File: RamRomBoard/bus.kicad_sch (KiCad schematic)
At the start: 4 parts, among them J1 BUS, J2 BUS, J3 Spare, J4 Spare

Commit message: New XC9572 Example
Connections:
- net RES6 is gone; now on net ~{CE_EXT1}: J2.5 (Pin_5), J4.5 (Pin_5)
- net RES0: now also J2.23 (Pin_23), J4.23 (Pin_23); no longer J2.11 (Pin_11), J4.11 (Pin_11)
- net RES1: now also J2.24 (Pin_24), J4.24 (Pin_24); no longer J2.10 (Pin_10), J4.10 (Pin_10)
- net RES2: now also J2.21 (Pin_21), J4.21 (Pin_21); no longer J2.9 (Pin_9), J4.9 (Pin_9)
- net RES3: now also J2.22 (Pin_22), J4.22 (Pin_22); no longer J2.8 (Pin_8), J4.8 (Pin_8)
- net RES4: now also J2.19 (Pin_19), J4.19 (Pin_19); no longer J2.7 (Pin_7), J4.7 (Pin_7)
- net RES5: now also J2.20 (Pin_20), J4.20 (Pin_20); no longer J2.6 (Pin_6), J4.6 (Pin_6)
- net ~{CE_EXT0}: now also J2.6 (Pin_6), J4.6 (Pin_6); no longer J2.12 (Pin_12), J4.12 (Pin_12)
- net ~{CE_EXT10}: now also J2.16 (Pin_16), J4.16 (Pin_16); no longer J2.22 (Pin_22), J4.22 (Pin_22)
- net ~{CE_EXT11}: now also J2.15 (Pin_15), J4.15 (Pin_15); no longer J2.23 (Pin_23), J4.23 (Pin_23)
- net ~{CE_EXT12}: now also J2.18 (Pin_18), J4.18 (Pin_18); no longer J2.24 (Pin_24), J4.24 (Pin_24)
- net ~{CE_EXT13}: now also J2.17 (Pin_17), J4.17 (Pin_17); no longer J2.25 (Pin_25), J4.25 (Pin_25)
- net ~{CE_EXT1}: no longer J2.13 (Pin_13), J4.13 (Pin_13)
- net ~{CE_EXT2}: now also J2.8 (Pin_8), J4.8 (Pin_8); no longer J2.14 (Pin_14), J4.14 (Pin_14)
- net ~{CE_EXT3}: now also J2.7 (Pin_7), J4.7 (Pin_7); no longer J2.15 (Pin_15), J4.15 (Pin_15)
- net ~{CE_EXT4}: now also J2.10 (Pin_10), J4.10 (Pin_10); no longer J2.16 (Pin_16), J4.16 (Pin_16)
- net ~{CE_EXT5}: now also J2.9 (Pin_9), J4.9 (Pin_9); no longer J2.17 (Pin_17), J4.17 (Pin_17)
- net ~{CE_EXT6}: now also J2.12 (Pin_12), J4.12 (Pin_12); no longer J2.18 (Pin_18), J4.18 (Pin_18)
- net ~{CE_EXT7}: now also J2.11 (Pin_11), J4.11 (Pin_11); no longer J2.19 (Pin_19), J4.19 (Pin_19)
- net ~{CE_EXT8}: now also J2.14 (Pin_14), J4.14 (Pin_14); no longer J2.20 (Pin_20), J4.20 (Pin_20)
- net ~{CE_EXT9}: now also J2.13 (Pin_13), J4.13 (Pin_13); no longer J2.21 (Pin_21), J4.21 (Pin_21)
- new net CLK1: J2.25 (Pin_25), J4.25 (Pin_25)
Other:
- note removed: "TDRTN must be connected to RES4 at the last board if a CPLD is mounted!"
- title: Unicomp v2 - RAMROM Board -> Unicomp v3 - RAMROM Board
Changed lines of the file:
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@@
 	(paper "A4")
 	(title_block
-		(title "Unicomp v2 - RAMROM Board")
-		(date "2023-07-06")
-		(rev "v1.4")
+		(title "Unicomp v3 - RAMROM Board")
+		(date "2024-05-13")
+		(rev "v1.0")
 		(company "100% Offner")
-		(comment 1 "      ~{uMWR} from A12 to A9 of STM32 bec. USB, MWR to R/~{W} on U1 Pin1")
-		(comment 2 "      WP doesnt work, changed to OR-Gate U3, U21C wrong,  ")
-		(comment 3 "      ~{CSRAM} directly to U1,  ~{RAMCSOR} new, Clock chip added")
-		(comment 4 "v1.3: Buffer for SCK and MOSI placed at output, internal signals directly to STM32")
+		(comment 1 "v1.0: Initial")
 	)
 	(bus_entry
@@
 	(wire
 		(pts
-			(xy 151.13 127) (xy 163.83 127)
+			(xy 151.13 127) (xy 162.56 127)
 		)
 		(stroke
@@
 	(wire
 		(pts
-			(xy 128.27 132.08) (xy 138.43 132.08)
-		)
-		(stroke
-			(width 0)
-			(type default)
-		)
-	)
-	(wire
-		(pts
 			(xy 90.17 57.15) (xy 104.14 57.15)
 		)
@@
 	(wire
 		(pts
-			(xy 151.13 132.08) (xy 158.75 132.08)
+			(xy 151.13 132.08) (xy 162.56 132.08)
 		)
 		(stroke
@@
 	(wire
 		(pts
-			(xy 63.5 34.29) (xy 77.47 34.29)
+			(xy 127 129.54) (xy 138.43 129.54)
 		)
 		(stroke
@@
 	(wire
 		(pts
-			(xy 144.78 34.29) (xy 151.13 34.29)
+			(xy 63.5 34.29) (xy 77.47 34.29)
 		)
 		(stroke
@@
 	(wire
 		(pts
-			(xy 128.27 134.62) (xy 138.43 134.62)
+			(xy 144.78 34.29) (xy 151.13 34.29)
 		)
 		(stroke
@@
 	(wire
 		(pts
-			(xy 128.27 129.54) (xy 138.43 129.54)
+			(xy 63.5 67.31) (xy 77.47 67.31)
 		)
 		(stroke
@@
 	(wire
 		(pts
-			(xy 63.5 67.31) (xy 77.47 67.31)
+			(xy 184.15 113.03) (xy 199.39 113.03)
 		)
 		(stroke
@@
 	(wire
 		(pts
-			(xy 184.15 113.03) (xy 199.39 113.03)
+			(xy 127 132.08) (xy 138.43 132.08)
 		)
 		(stroke
@@
 	(wire
 		(pts
+			(xy 127 134.62) (xy 138.43 134.62)
+		)
+		(stroke
+			(width 0)
+			(type default)
+		)
+	)
+	(wire
+		(pts
 			(xy 39.37 93.98) (xy 34.29 93.98)
 		)
@@
 	(wire
 		(pts
-			(xy 151.13 134.62) (xy 158.75 134.62)
+			(xy 151.13 134.62) (xy 162.56 134.62)
 		)
 		(stroke
@@
 		)
 	)
-	(text "TDRTN must be connected \nto RES4 at the last board\nif a CPLD is mounted!"
-		(exclude_from_sim no)
-		(at 163.83 147.32 0)
-		(effects
-			(font
-				(size 1.27 1.27)
-			)
-			(justify left bottom)
-		)
-	)
 	(label "D7"
 		(at 63.5 46.99 0)
@@
 	)
 	(label "~{CE_EXT8}"
-		(at 64.77 116.84 0)
+		(at 64.77 124.46 0)
 		(fields_autoplaced yes)
 		(effects
@@
 	)
 	(label "~{CE_EXT1}"
-		(at 102.87 124.46 180)
-		(fields_autoplaced yes)
-		(effects
-			(font
-				(size 1.27 1.27)
-			)
-			(justify right bottom)
-		)
-	)
-	(label "RES6"
 		(at 102.87 134.62 180)
 		(fields_autoplaced yes)
@@
 	)
 	(label "~{CE_EXT6}"
-		(at 64.77 119.38 0)
+		(at 64.77 127 0)
 		(fields_autoplaced yes)
 		(effects
@@
 	)
 	(label "~{CE_EXT5}"
-		(at 162.56 119.38 180)
+		(at 162.56 129.54 180)
 		(fields_autoplaced yes)
 		(effects
@@
 	)
 	(label "~{CE_EXT1}"
-		(at 162.56 124.46 180)
+		(at 162.56 134.62 180)
 		(fields_autoplaced yes)
 		(effects
@@
 	)
 	(label "RES5"
-		(at 64.77 134.62 0)
+		(at 64.77 116.84 0)
 		(fields_autoplaced yes)
 		(effects
@@
 	)
 	(label "~{CE_EXT8}"
-		(at 127 116.84 0)
+		(at 127 124.46 0)
 		(fields_autoplaced yes)
 		(effects
@@
 	)
 	(label "~{CE_EXT13}"
-		(at 102.87 109.22 180)
+		(at 102.87 119.38 180)
 		(fields_autoplaced yes)
 		(effects
@@
 	)
 	(label "~{CE_EXT4}"
-		(at 64.77 121.92 0)
+		(at 64.77 129.54 0)
 		(fields_autoplaced yes)
 		(effects
@@
 	)
 	(label "~{CE_EXT13}"
-		(at 162.56 109.22 180)
+		(at 162.56 119.38 180)
 		(fields_autoplaced yes)
 		(effects
@@
 		)
 	)
+	(label "CLK1"
+		(at 102.87 109.22 180)
+		(fields_autoplaced yes)
+		(effects
+			(font
+				(size 1.27 1.27)
+			)
+			(justify right bottom)
+		)
+	)
 	(label "~{CE_EXT5}"
-		(at 102.87 119.38 180)
+		(at 102.87 129.54 180)
 		(fields_autoplaced yes)
 		(effects
@@
 	)
 	(label "~{CE_EXT6}"
-		(at 127 119.38 0)
+		(at 127 127 0)
 		(fields_autoplaced yes)
 		(effects
@@
 	)
 	(label "~{CE_EXT0}"
-		(at 127 127 0)
+		(at 127 134.62 0)
 		(fields_autoplaced yes)
 		(effects
@@
 	)
 	(label "~{CE_EXT12}"
-		(at 127 111.76 0)
+		(at 127 119.38 0)
 		(fields_autoplaced yes)
 		(effects
@@
 	)
 	(label "~{CE_EXT0}"
-		(at 64.77 127 0)
+		(at 64.77 134.62 0)
 		(fields_autoplaced yes)
 		(effects
@@
 	)
 	(label "~{CE_EXT7}"
-		(at 102.87 116.84 180)
+		(at 102.87 127 180)
 		(fields_autoplaced yes)
 		(effects
@@
 	)
 	(label "RES4"
-		(at 102.87 132.08 180)
+		(at 102.87 116.84 180)
 		(fields_autoplaced yes)
 		(effects
@@
 	)
 	(label "~{CE_EXT3}"
-		(at 102.87 121.92 180)
+		(at 102.87 132.08 180)
 		(fields_autoplaced yes)
 		(effects
@@
 	)
 	(label "RES1"
-		(at 64.77 129.54 0)
+		(at 64.77 111.76 0)
 		(fields_autoplaced yes)
 		(effects
@@
 	)
 	(label "~{CE_EXT2}"
-		(at 127 124.46 0)
+		(at 127 132.08 0)
 		(fields_autoplaced yes)
 		(effects
@@
 	)
 	(label "~{CE_EXT9}"
-		(at 162.56 114.3 180)
+		(at 162.56 124.46 180)
 		(fields_autoplaced yes)
 		(effects
@@
 	)
 	(label "~{CE_EXT10}"
-		(at 127 114.3 0)
+		(at 127 121.92 0)
 		(fields_autoplaced yes)
 		(effects
@@
 	)
 	(label "RES2"
-		(at 102.87 129.54 180)
+		(at 102.87 114.3 180)
 		(fields_autoplaced yes)
 		(effects
@@
 	)
 	(label "~{CE_EXT7}"
-		(at 162.56 116.84 180)
+		(at 162.56 127 180)
 		(fields_autoplaced yes)
 		(effects
@@
 	)
 	(label "~{CE_EXT10}"
-		(at 64.77 114.3 0)
+		(at 64.77 121.92 0)
 		(fields_autoplaced yes)
 		(effects
@@
 	)
 	(label "~{CE_EXT11}"
-		(at 162.56 111.76 180)
+		(at 162.56 121.92 180)
 		(fields_autoplaced yes)
 		(effects
@@
 	)
 	(label "~{CE_EXT11}"
-		(at 102.87 111.76 180)
+		(at 102.87 121.92 180)
 		(fields_autoplaced yes)
 		(effects
@@
 	)
 	(label "~{CE_EXT2}"
-		(at 64.77 124.46 0)
+		(at 64.77 132.08 0)
 		(fields_autoplaced yes)
 		(effects
@@
 	)
 	(label "~{CE_EXT12}"
-		(at 64.77 111.76 0)
+		(at 64.77 119.38 0)
 		(fields_autoplaced yes)
 		(effects
@@
 	)
 	(label "~{CE_EXT3}"
-		(at 162.56 121.92 180)
+		(at 162.56 132.08 180)
 		(fields_autoplaced yes)
 		(effects
@@
 	)
 	(label "RES3"
-		(at 64.77 132.08 0)
+		(at 64.77 114.3 0)
 		(fields_autoplaced yes)
 		(effects
@@
 	)
 	(label "RES0"
-		(at 102.87 127 180)
+		(at 102.87 111.76 180)
 		(fields_autoplaced yes)
 		(effects
@@
 	)
 	(label "~{CE_EXT4}"
-		(at 127 121.92 0)
+		(at 127 129.54 0)
 		(fields_autoplaced yes)
 		(effects
@@
 	)
 	(label "~{CE_EXT9}"
-		(at 102.87 114.3 180)
+		(at 102.87 124.46 180)
 		(fields_autoplaced yes)
 		(effects
@@
 	(hierarchical_label "RES1"
 		(shape output)
-		(at 128.27 129.54 180)
+		(at 127 111.76 180)
 		(fields_autoplaced yes)
 		(effects
@@
 	(hierarchical_label "RES5"
 		(shape output)
-		(at 128.27 134.62 180)
+		(at 127 116.84 180)
 		(fields_autoplaced yes)
 		(effects
@@
 		)
 	)
+	(hierarchical_label "CLK1"
+		(shape output)
+		(at 162.56 109.22 0)
+		(fields_autoplaced yes)
+		(effects
+			(font
+				(size 1.27 1.27)
+			)
+			(justify left)
+		)
+	)
 	(hierarchical_label "RX1"
 		(shape input)
@@
 	(hierarchical_label "RES0"
 		(shape output)
-		(at 163.83 127 0)
+		(at 162.56 111.76 0)
 		(fields_autoplaced yes)
 		(effects
@@
 	(hierarchical_label "RES2"
 		(shape output)
-		(at 162.56 129.54 0)
+		(at 162.56 114.3 0)
 		(fields_autoplaced yes)
 		(effects
@@
 	(hierarchical_label "RES4"
 		(shape output)
-		(at 158.75 132.08 0)
+		(at 162.56 116.84 0)
 		(fields_autoplaced yes)
 		(effects
@@
 	(hierarchical_label "RES3"
 		(shape output)
-		(at 128.27 132.08 180)
+		(at 127 114.3 180)
 		(fields_autoplaced yes)
 		(effects
@@
 		(fields_autoplaced yes)
 		(effects
-			(font
-				(size 1.27 1.27)
-			)
-			(justify left)
-		)
-	)
-	(hierarchical_label "RES6"
-		(shape input)
-		(at 158.75 134.62 0)
-		(fields_autoplaced yes)
-		(effects

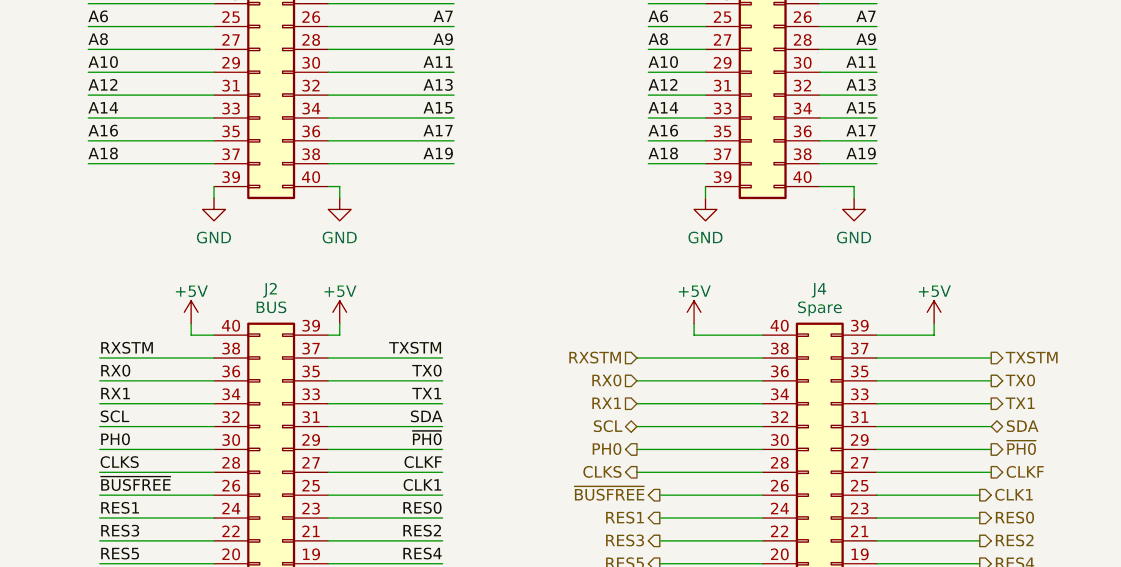
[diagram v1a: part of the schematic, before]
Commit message: Schematics of RAMROM Board updated
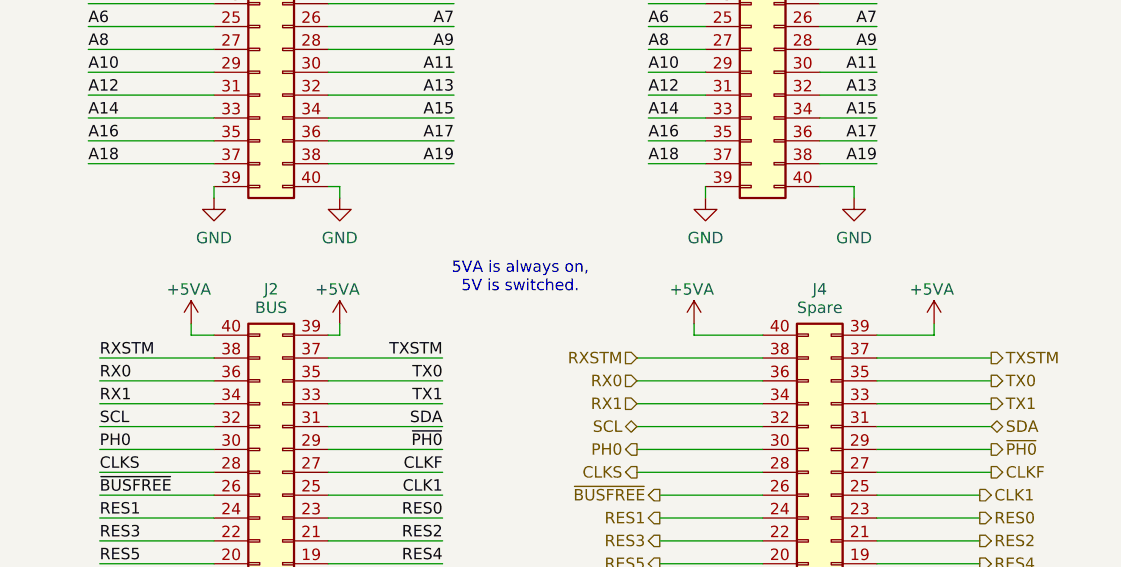
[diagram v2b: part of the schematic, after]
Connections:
- net +5V: no longer J2.39 (Pin_39), J2.40 (Pin_40), J4.39 (Pin_39), J4.40 (Pin_40)
- new net +5VA: J2.39 (Pin_39), J2.40 (Pin_40), J4.39 (Pin_39), J4.40 (Pin_40)
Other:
- note added: "5VA is always on, 5V is switched."

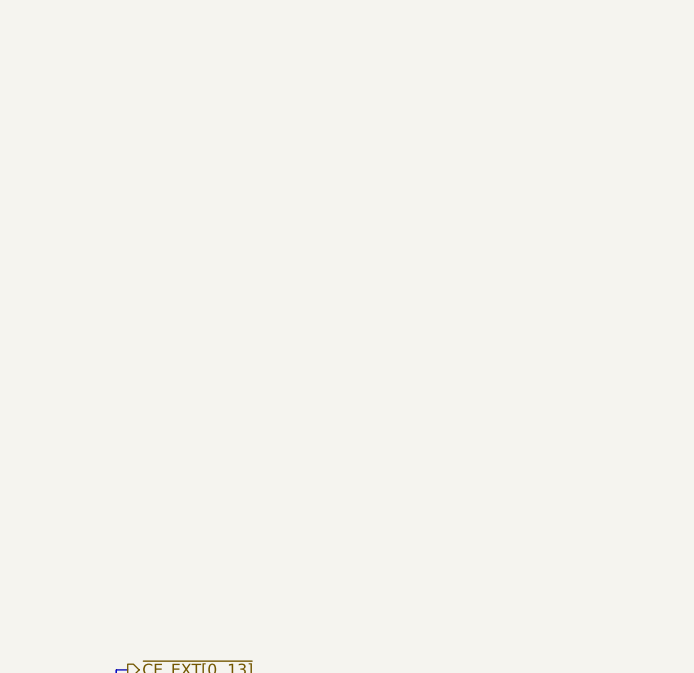
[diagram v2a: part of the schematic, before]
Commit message: Diodes on Databus added, DS1314 different footprint
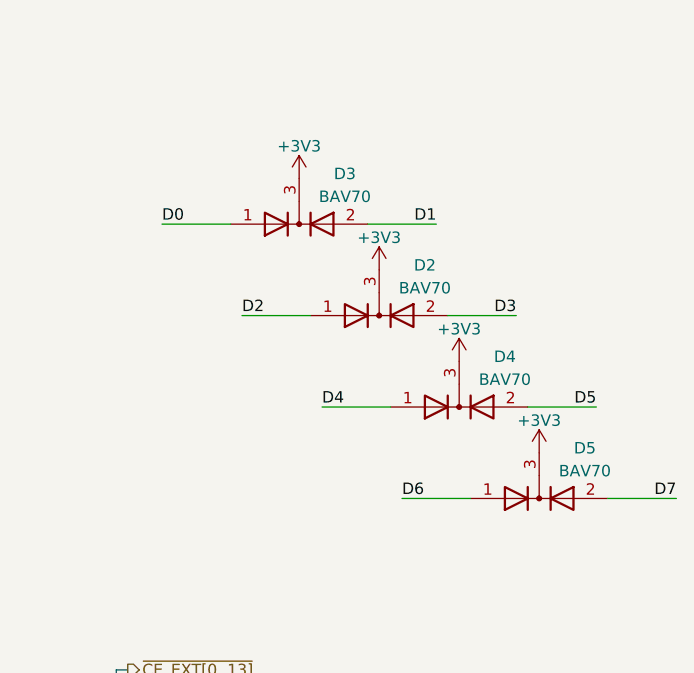
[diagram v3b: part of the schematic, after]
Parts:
- added D2, D3, D4, D5: BAV70, Package_TO_SOT_SMD:SOT-23, symbol Diode:BAV70
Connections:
- net +3V3: now also D2.3 (K), D3.3 (K), D4.3 (K), D5.3 (K)
- net D0: now also D3.1 (A)
- net D1: now also D3.2 (A)
- net D2: now also D2.1 (A)
- net D3: now also D2.2 (A)
- net D4: now also D4.1 (A)
- net D5: now also D4.2 (A)
- net D6: now also D5.1 (A)
- net D7: now also D5.2 (A)

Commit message: many new boards
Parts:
- added D10, D11, D6, D7, D8, D9: BAV70, Package_TO_SOT_SMD:SOT-23, symbol Diode:BAV70
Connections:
- net +3V3: now also D10.3 (K), D11.3 (K), D6.3 (K), D7.3 (K), D8.3 (K), D9.3 (K)
- net A0: now also D4.1 (A)
- net A1: now also D3.2 (A)
- net A10: now also D9.2 (A)
- net A11: now also D8.1 (A)
- net A12: now also D8.2 (A)
- net A13: now also D7.1 (A)
- net A14: now also D7.2 (A)
- net A15: now also D6.1 (A)
- net A16: now also D6.2 (A)
- net A17: now also D5.2 (A)
- net A18: now also D5.1 (A)
- net A19: now also D4.2 (A)
- net A2: now also D3.1 (A)
- net A3: now also D2.2 (A)
- net A4: now also D2.1 (A)
- net A5: now also D11.1 (A)
- net A6: now also D11.2 (A)
- net A7: now also D10.1 (A)
- net A8: now also D10.2 (A)
- net A9: now also D9.1 (A)
- net D0: no longer D3.1 (A)
- net D1: no longer D3.2 (A)
- net D2: no longer D2.1 (A)
- net D3: no longer D2.2 (A)
- net D4: no longer D4.1 (A)
- net D5: no longer D4.2 (A)
- net D6: no longer D5.1 (A)
- net D7: no longer D5.2 (A)
- net RES0 renamed ~{STM32BUS}

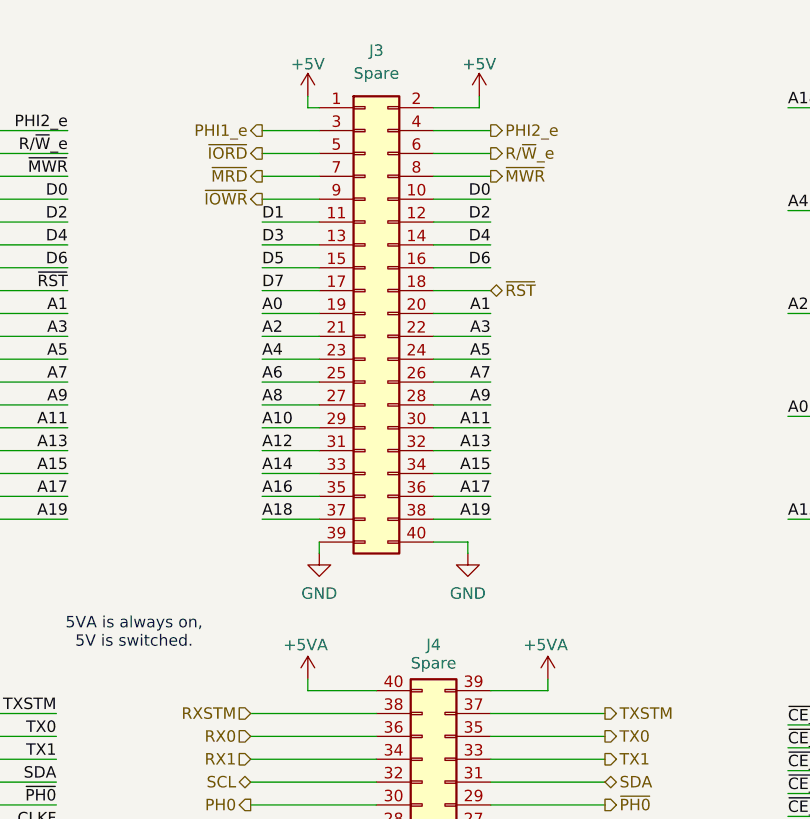
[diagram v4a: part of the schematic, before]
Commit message: first boards manufactured
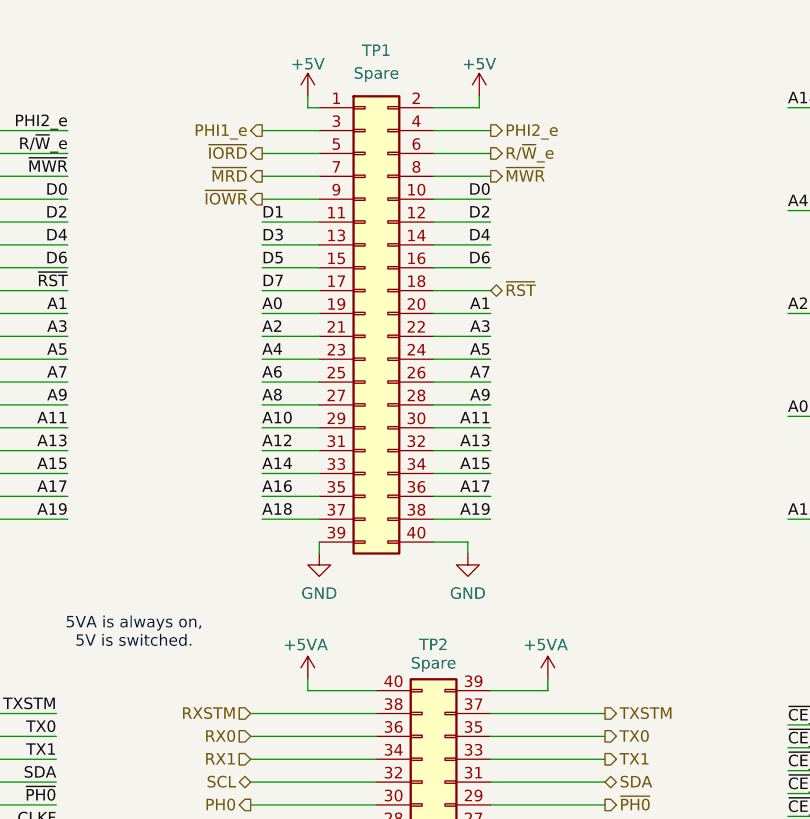
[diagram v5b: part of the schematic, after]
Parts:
- renumbered J3 to TP1, J4 to TP2
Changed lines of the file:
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@@
 		(on_board yes)
 		(dnp no)
-		(property "Reference" "J4"
+		(property "Reference" "TP2"
 			(at 144.78 86.344 0)
 			(effects
@@
 			(project "RamRomBoard"
 				(path "/2eaa3998-c9cb-43b1-9b23-df656c8158b0/9272637d-1dcb-4eb8-96b5-e029cf524af1"
-					(reference "J4")
+					(reference "TP2")
 					(unit 1)
 				)
@@
 		(dnp no)
 		(fields_autoplaced yes)
-		(property "Reference" "J3"
+		(property "Reference" "TP1"
 			(at 138.43 20.32 0)
 			(effects
@@
 			(project "RamRomBoard"
 				(path "/2eaa3998-c9cb-43b1-9b23-df656c8158b0/9272637d-1dcb-4eb8-96b5-e029cf524af1"
-					(reference "J3")
-					(unit 1)
-				)
+					(reference "TP1")
+					(unit 1)
+				)
